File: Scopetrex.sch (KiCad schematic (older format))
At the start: 47 parts, among them J201 CART, SW201 SW_TACT, U201 AT28C64B, U202 74LS00, U203 74LS32, U204 AS6C62256, U205 AY3-8910, U206 MC68A09, U207 W65C22S6TPG, U208 AY3-8912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

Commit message: better part for right angle cart slot
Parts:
- J201: Digikey S3311-ND -> A139219-ND
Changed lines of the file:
@@
 F 3 "~" H 1350 2400 50  0001 C CNN
 F 4 "587-395-036" H 0   0   50  0001 C CNN "Mouser"
-F 5 "S3311-ND" H 1350 2400 50  0001 C CNN "Digikey"
+F 5 "A139219-ND" H 1350 2400 50  0001 C CNN "Digikey"
 	1    1350 2400
 	1    0    0    -1
@@
 Wire Notes Line
 	2350 3150 2350 4400
-Wire Bus Line
-	550  600  550  2600
-Wire Bus Line
-	2150 500  2150 2200
-Wire Bus Line
-	2200 600  2200 2700
-Wire Bus Line
-	6100 500  6100 3750
-Wire Bus Line
-	6500 3700 6500 4850
-Wire Bus Line
-	800  500  800  3100
-Wire Bus Line
-	5950 600  5950 3700
-Wire Bus Line
-	3050 600  3050 1800
-Wire Bus Line
-	7650 600  7650 1800
-Wire Bus Line
-	9600 600  9600 2450
-Wire Bus Line
-	8000 600  8000 2350
-Wire Bus Line
-	6650 3750 6650 5150
-Wire Bus Line
-	8050 3700 8050 4850
-Wire Bus Line
-	5100 3750 5100 5350
-Wire Bus Line
-	5000 500  5000 2600
 Text Notes 9100 7100 0    50   ~ 0
 This work is licensed under the Creative Commons\nAttribution-ShareAlike 4.0 International License.\nTo view a copy of this license, visit \nhttp://creativecommons.org/licenses/by-sa/4.0/\nor send a letter to Creative Commons, PO Box 1866,\nMountain View, CA 94042, USA.
@@
 Text Notes 7150 6950 0    50   ~ 0
 Digital Section\nBy @TubeTimeUS
+Wire Bus Line
+	550  600  550  2600
+Wire Bus Line
+	2150 500  2150 2200
+Wire Bus Line
+	2200 600  2200 2700
+Wire Bus Line
+	6100 500  6100 3750
+Wire Bus Line
+	6500 3700 6500 4850
+Wire Bus Line
+	800  500  800  3100
+Wire Bus Line
+	5950 600  5950 3700
+Wire Bus Line
+	3050 600  3050 1800
+Wire Bus Line
+	7650 600  7650 1800
+Wire Bus Line
+	9600 600  9600 2450
+Wire Bus Line
+	8000 600  8000 2350
+Wire Bus Line
+	6650 3750 6650 5150
+Wire Bus Line
+	8050 3700 8050 4850
+Wire Bus Line
+	5100 3750 5100 5350
+Wire Bus Line
+	5000 500  5000 2600
 $EndSCHEMATC

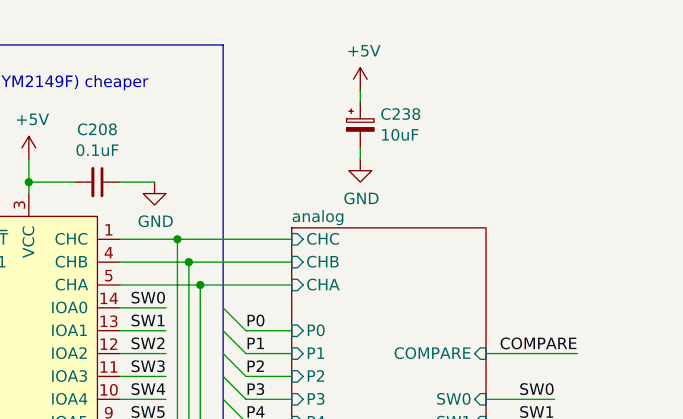
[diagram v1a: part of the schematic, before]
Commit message: Fix FB201 value and change C238 to 22uF
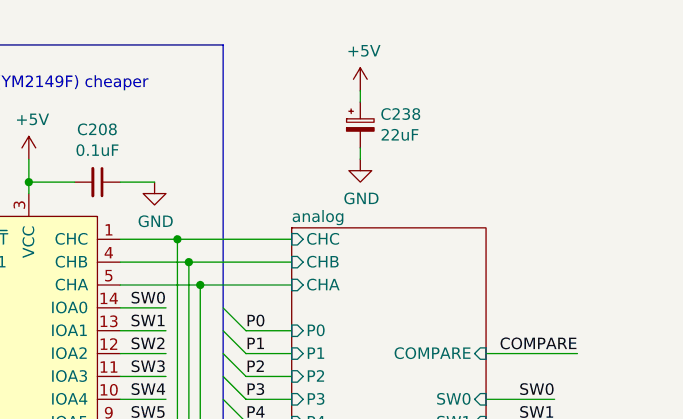
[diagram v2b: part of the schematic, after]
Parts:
- C238: value 10uF -> 22uF
- FB201: value Ferrite_Bead_Small -> 96Ω @ 25MHz
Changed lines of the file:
@@
 P 10200 950
 F 0 "C238" H 10288 996 50  0000 L CNN
-F 1 "10uF" H 10288 905 50  0000 L CNN
+F 1 "22uF" H 10288 905 50  0000 L CNN
 F 2 "Passive:CAPAP200" H 10200 950 50  0001 C CNN
 F 3 "~" H 10200 950 50  0001 C CNN
@@
 P 1700 1200
 F 0 "FB201" H 1350 1200 50  0000 L CNN
-F 1 "Ferrite_Bead_Small" H 1800 1155 50  0001 L CNN
+F 1 "96Ω @ 25MHz" H 1800 1155 50  0001 L CNN
 F 2 "Passive:FB254" V 1630 1200 50  0001 C CNN
 F 3 "~" H 1700 1200 50  0001 C CNN
